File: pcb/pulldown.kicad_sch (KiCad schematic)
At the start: 1 part, among them Q12 BC817

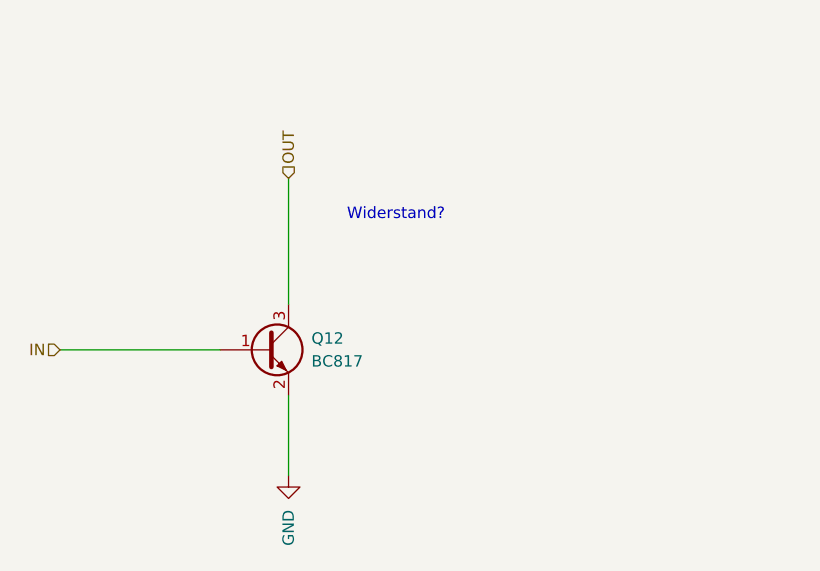
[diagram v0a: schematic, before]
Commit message: added some diodes, fuses etc
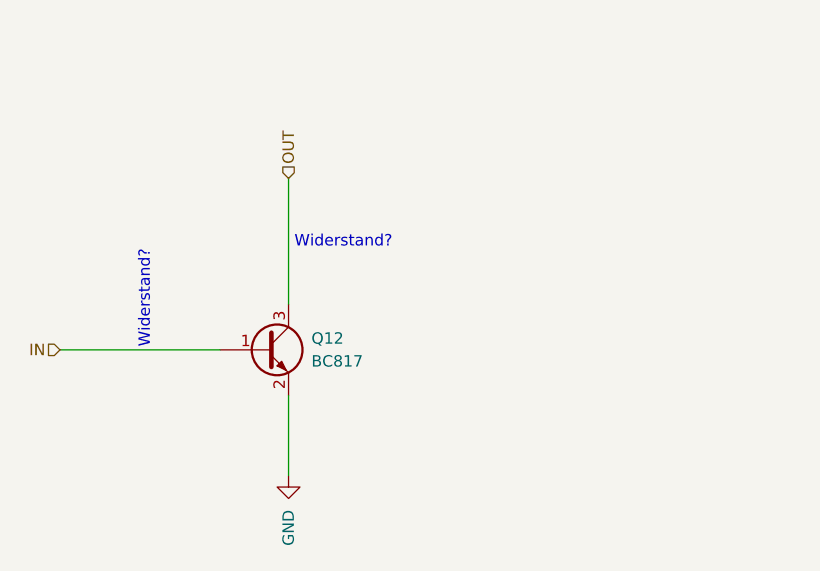
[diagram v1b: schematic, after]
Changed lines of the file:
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@@
 	(text "Widerstand?"
 		(exclude_from_sim no)
-		(at 145.288 81.534 0)
+		(at 117.348 90.932 90)
 		(effects
 			(font
+				(size 1.27 1.27)
+			)
+		)
+	)
+	(text "Widerstand?"
+		(exclude_from_sim no)
+		(at 139.446 84.582 0)
+		(effects
+			(font

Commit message: major work
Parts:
- added R39, R40: 10k, Resistor_SMD:R_0603_1608Metric, symbol Device:R
- added R41: 750, Resistor_THT:R_Axial_DIN0207_L6.3mm_D2.5mm_P7.62mm_Horizontal, symbol Device:R
- renumbered Q12 to Q3
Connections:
- net GND: now also R40.1
- net IN: now also R39.1; no longer Q3.1 (B)
- net OUT: now also R41.1; no longer Q3.3 (C)
- new net: Q3.1 (B), R39.2, R40.2
- new net: Q3.3 (C), R41.2
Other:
- note added: "310mW max power dissipation => 0.310mW / 11 V = 0.028 Ar => 0.310mW / 15 V = 0.021 Ar => 11 V / 0.028 A = 392R => 15 V / 0.021 A = 714R"
- note added: "richtiger Widerstand?"
- note removed: "Widerstand?"

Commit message: edit pulldown
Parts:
- removed Q3: BC817, Package_TO_SOT_SMD:SOT-23, symbol Transistor_BJT:BC817
- added JP4: Jumper_2_Open, Jumper:SolderJumper-2_P1.3mm_Open_Pad1.0x1.5mm, symbol Jumper:Jumper_2_Open
- added Q3: 2SC1623 300-400, lcsc:SOT-23-3_L2.9-W1.3-P1.90-LS2.4-BR, symbol lcsc:2SC1623300-400
- added R39: DNP, Resistor_THT:R_Axial_DIN0207_L6.3mm_D2.5mm_P7.62mm_Horizontal, symbol Device:R
- R41: value 750 -> 1k5
- renumbered R39 to R46
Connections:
- net GND: now also Q3.2 (E)
- net OUT: now also R41.2, Q3.3 (C), R39.2; no longer R41.1
- net at R40.2, R46.2: now also Q3.1 (B)
- new net: JP4.1 (A), R41.1
- new net +12V: JP4.2 (B), R39.1
